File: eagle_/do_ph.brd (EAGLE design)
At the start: 100 x 80.6 mm, 25 parts, among them IC1 MEGA8-P, Q1 8Mhz

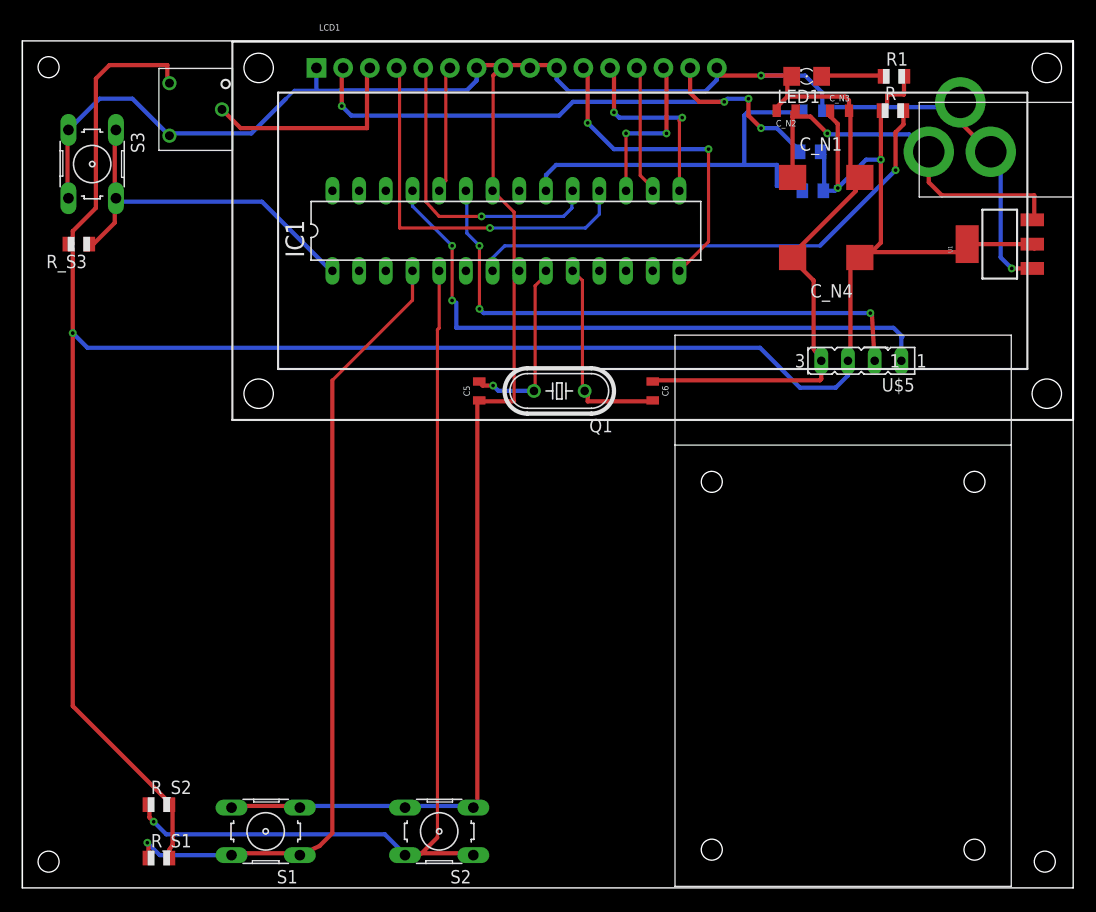
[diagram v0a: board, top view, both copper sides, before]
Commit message: thêm jack nap code
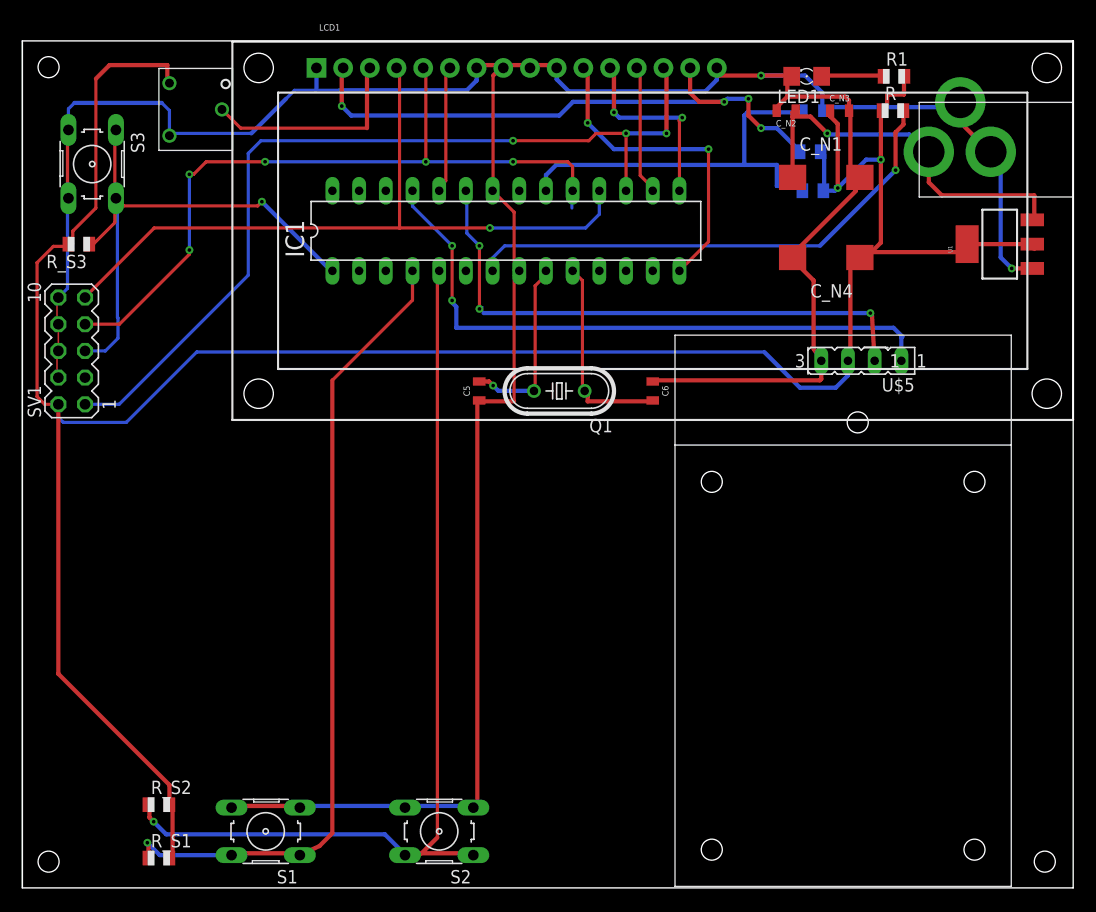
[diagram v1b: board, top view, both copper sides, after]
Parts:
- added SV1: (no value), con-lstb:MA05-2
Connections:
- net D7: now also SV1.1
- net GND: now also SV1.10, SV1.4, SV1.6, SV1.8
- net RS: now also SV1.9
- net RST: now also SV1.5
- net RW: now also SV1.7
- net VCC: now also SV1.2
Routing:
- net D7: track 15.7 -> 84.9 mm, vias 2 -> 3
- net RW: track 29.4 -> 70.7 mm, vias 1 -> 5
- net RS: track 37.2 -> 69.8 mm
- net GND: track 288.1 -> 308.5 mm
- net RST: track 35.6 -> 52.9 mm, vias 0 -> 1
- net VCC: track 232.7 -> 243.0 mm, vias 3 -> 2

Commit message: update
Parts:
- moved U$5 18.0 mm to (86.5, 29.4), turned to 180 degrees
- moved S1 12.9 mm to (15.3, 15.5)
- moved S2 12.9 mm to (31.8, 15.5)
- moved R_S1 12.9 mm to (5.10, 12.9)
- moved R_S2 12.9 mm to (5.10, 18.0)
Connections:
- new net RX: IC1.2, SV1.4
- new net TX: IC1.3, SV1.6
- net GND: no longer SV1.4, SV1.6
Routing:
- net ADC_1: track 54.2 -> 98.5 mm
- net TX: track 0.00 -> 37.9 mm
- net RX: track 0.00 -> 37.4 mm
- net ADC_2: track 60.0 -> 43.0 mm, vias 2 -> 3
- net START: track 77.1 -> 69.9 mm
- net START2: track 89.9 -> 82.6 mm
- net VCC: track 243.0 -> 250.2 mm, vias 2 -> 3
- net GND: track 308.5 -> 302.9 mm
- net RW: track 70.7 -> 69.1 mm

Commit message: update
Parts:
- removed S3: (no value), switch-omron:B3F-10XX
- removed SV1: (no value), con-lstb:MA05-2
- removed U$6: RM065_V1, RM065:RM065
- added RST: (no value), switch-omron:B3F-10XX
- added SV2: (no value), con-lsta:FE07-2
- added U$2: RES_RM063, res_RM063:RM063
- moved R_S3 56.0 mm to (34.0, 13.0), turned to 0 degrees
- moved R_S2 30.0 mm to (34.0, 9.80), turned to 180 degrees
- moved R_S1 29.1 mm to (34.0, 16.5), turned to 180 degrees
- moved S1 26.8 mm to (42.0, 14.0), turned to 90 degrees
- moved S2 20.3 mm to (52.0, 14.0), turned to 270 degrees
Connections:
- net D7: now also SV2.6; no longer SV1.1
- net GND: now also RST.3, RST.4, SV2.11, SV2.13, SV2.7, SV2.9, U$2.P$2; no longer S3.3, S3.4, SV1.10, SV1.8, U$6.P$2
- net N$1: now also U$2.P$3; no longer U$6.P$3
- net RS: now also SV2.14; no longer SV1.9
- net RST: now also RST.1, RST.2, SV2.10; no longer S3.1, S3.2, SV1.5
- net RW: now also SV2.12; no longer SV1.7
- net RX: now also SV2.1; no longer SV1.4
- net TX: now also SV2.3; no longer SV1.6
- net VCC: now also SV2.5, U$2.P$1; no longer SV1.2, U$6.P$1
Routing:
- net ADC_1: track 98.5 -> 44.9 mm, vias 3 -> 2
- net VCC: track 250.2 -> 215.2 mm, vias 3 -> 5
- net RS: track 69.8 -> 87.7 mm, vias 1 -> 2
- net RST: track 52.9 -> 68.9 mm, vias 1 -> 3
- net START: track 69.9 -> 54.1 mm
- net RW: track 69.1 -> 84.9 mm, vias 5 -> 3
- net RX: track 37.4 -> 23.5 mm
- net GND: track 302.9 -> 290.6 mm
- net TX: track 37.9 -> 26.9 mm
- net N$1: track 20.4 -> 14.8 mm
- net ADC_2: track 43.0 -> 42.2 mm, vias 3 -> 2
- net D7: track 84.9 -> 84.2 mm, vias 3 -> 4
- net START2: track 82.6 -> 83.2 mm, vias 1 -> 2
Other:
- board size 100 x 80.6 mm -> 80.3 x 73.6 mm

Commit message: update
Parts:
- removed C5, C6: 22pF, SparkFun-Capacitors:0805
- added C1, C2: 22pF, SparkFun-Retired:0402-CAP
- moved R_S1 1.41 mm to (34.2, 17.9)
- moved R_S3 0.92 mm to (34.2, 13.9), turned to 180 degrees
- moved R_S2 0.28 mm to (34.2, 10.0)
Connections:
- net GND: now also C1.1, C2.1; no longer C5.1, C6.1
- net XTA1: now also C1.2; no longer C5.2
- net XTA2: now also C2.2; no longer C6.2
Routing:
- net START2: track 83.2 -> 74.2 mm
- net RST: track 68.9 -> 74.6 mm, vias 3 -> 4
- net VCC: track 215.2 -> 210.2 mm, vias 5 -> 4
- net N$11: track 49.0 -> 52.8 mm
- net XTA2: track 19.3 -> 16.6 mm
- net N$2: track 36.7 -> 34.1 mm
- net N$6: track 39.1 -> 36.7 mm
- net START: track 54.1 -> 51.8 mm, vias 1 -> 0
- net RS: track 87.7 -> 89.9 mm
- net VO: track 57.9 -> 56.2 mm, vias 4 -> 3
- net D7: track 84.2 -> 85.4 mm
- net GND: track 290.6 -> 291.6 mm, vias 2 -> 4
- net RW: track 84.9 -> 83.9 mm

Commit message: update
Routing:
- net GND: track 291.6 -> 291.1 mm
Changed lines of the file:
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@@
 <wire x1="79" y1="67.5" x2="79.4" y2="67.31" width="0.4064" layer="1"/>
 <wire x1="78.5" y1="73.5" x2="78.37" y2="73.66" width="0.4064" layer="1"/>
-<wire x1="79" y1="67" x2="79.4" y2="67.31" width="0.4064" layer="1"/>
 <wire x1="45" y1="78" x2="43" y2="78" width="0.4064" layer="1"/>
 <wire x1="43" y1="78" x2="42.93" y2="77.73" width="0.4064" layer="1"/>
@@
 <wire x1="21.5" y1="73.5" x2="24.65" y2="73.5" width="0.3048" layer="16"/>
 <wire x1="24.65" y1="73.5" x2="26.25" y2="71.9" width="0.3048" layer="16"/>
-<wire x1="76.26" y1="66.04" x2="75.93" y2="66.04" width="0.3048" layer="16"/>
 <wire x1="33.03" y1="28.67" x2="33" y2="28.7" width="0.3048" layer="16"/>
 <via x="33" y="28.7" extent="1-16" drill="0.35"/>
@@
 <contactref element="L" pad="2"/>
 <contactref element="C4" pad="1"/>
-<wire x1="74.03" y1="73.66" x2="74" y2="73.5" width="0.4064" layer="16"/>
 <wire x1="50.6" y1="68.6" x2="68.4" y2="68.6" width="0.3048" layer="16"/>
 <wire x1="49.53" y1="66.04" x2="49.53" y2="67.53" width="0.4064" layer="16"/>
